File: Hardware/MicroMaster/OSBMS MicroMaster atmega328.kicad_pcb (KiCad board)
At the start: 2 copper layers, 33 parts, among them IC1 ATMEGA328P-A, P1 CONN_01X06, P10 CONN_01X04, P11 CONN_01X04, P2 CONN_02X03, P3 CONN_01X03, P4 CONN_01X03, P6 CONN_01X03, P7 CONN_01X02, P8 CONN_01X04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

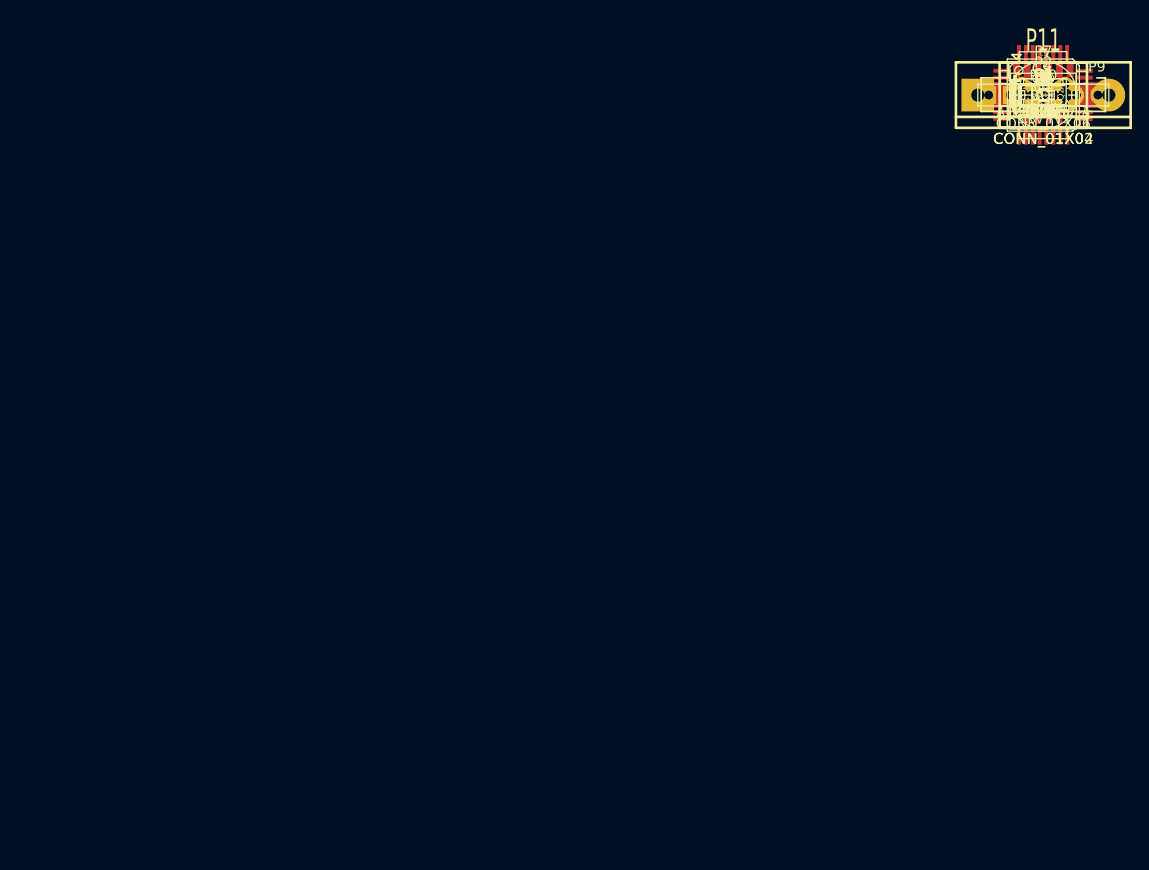
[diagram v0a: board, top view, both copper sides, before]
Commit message: touched up balancer board and reorganised
touched up balancer board so that it is ready for production,
reorganised a bunch of files and added proper revision labels, and made
good progress on the micromaster board. the schematic is complete, the
board is layed out, some traces still need to be run though.
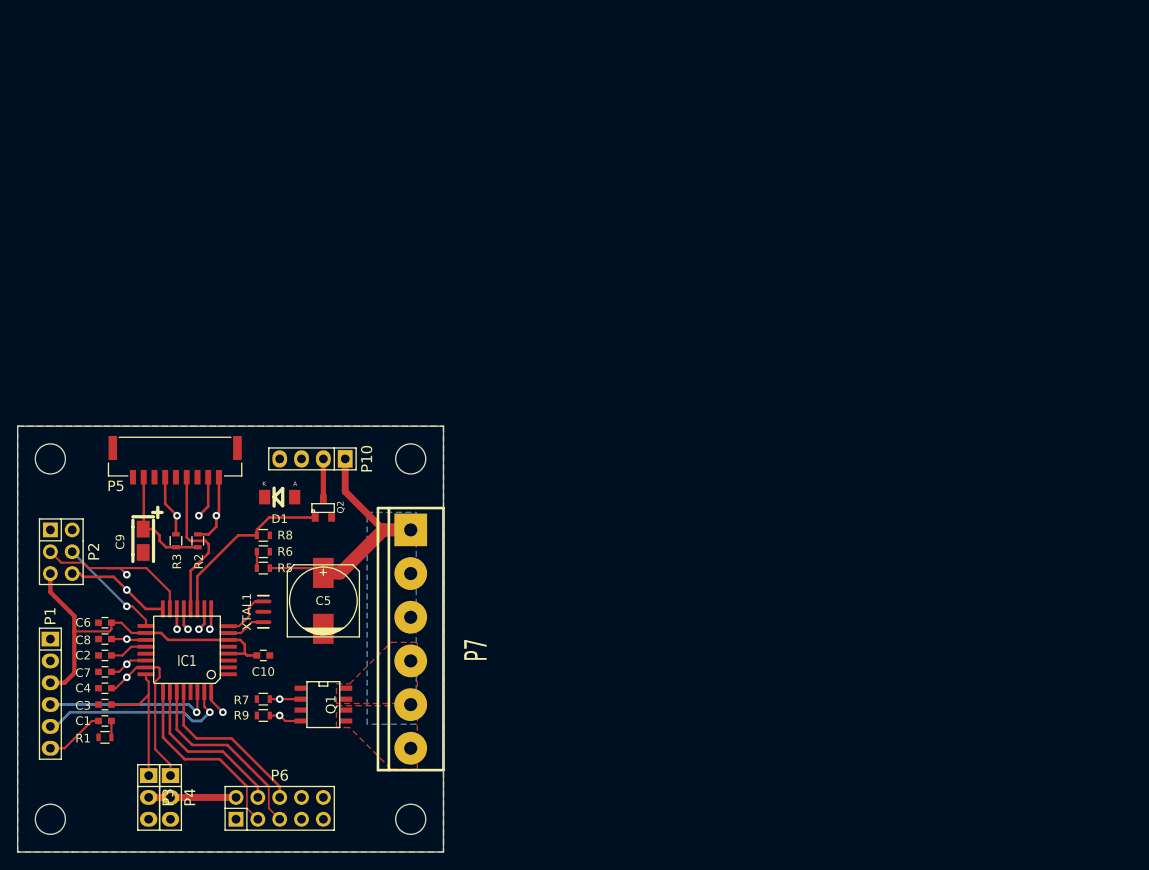
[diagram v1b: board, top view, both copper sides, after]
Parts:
- removed P11: CONN_01X04, Connect:bornier4
- removed P8: CONN_01X04, Pin_Headers:Pin_Header_Straight_1x04
- removed P9: CONN_01X06, Connectors_Molex:Connector_Molex_PicoBlade_53261-0671
- removed R4: 4.7K, Resistors_SMD:R_0603
- added MH: MountingHole_3-5mm_RevA_Date21Jun2010, Mounting_Holes:MountingHole_3-5mm, F.Cu at (71.1, 174.0)
- added MH: MountingHole_3-5mm_RevA_Date21Jun2010, Mounting_Holes:MountingHole_3-5mm, F.Cu at (29.2, 174.0)
- added MH: MountingHole_3-5mm_RevA_Date21Jun2010, Mounting_Holes:MountingHole_3-5mm, F.Cu at (29.2, 132.1)
- added MH: MountingHole_3-5mm_RevA_Date21Jun2010, Mounting_Holes:MountingHole_3-5mm, F.Cu at (71.1, 132.1)
- added P5: CONN_01X09, MyCustomParts:Connector_SMD_GH_SIDECONN_1X9_1.25MM_45515711ND, F.Cu at (43.8, 130.8)
- added XTAL1: 8mhz resonator, RESONATOR-SMD, F.Cu at (54.0, 149.9)
- D1: footprint SMD_Packages:DO-214-AC_SMA -> Diodes_SMD:Diode-MiniMELF_Standard
- IC1: footprint SMD_Packages:TQFP-32 -> TQFP-32
- P6: value CONN_01X03 -> CONN_01X10; footprint Pin_Headers:Pin_Header_Straight_1x03 -> Pin_Headers:Pin_Header_Straight_2x05
- P7: value CONN_01X02 -> CONN_01X06; footprint Connect:bornier2 -> Connect:bornier6
- moved P1 134.8 mm to (29.2, 159.4), turned to 270 degrees
- moved P3 132.3 mm to (40.6, 171.4), turned to 270 degrees
- moved R1 132.2 mm to (35.6, 164.5), turned to 180 degrees
- moved C1 131.2 mm to (35.6, 162.6)
- moved P4 130.3 mm to (43.2, 171.4), turned to 270 degrees
- moved C3 130.1 mm to (35.6, 160.7)
- moved C4 129.1 mm to (35.6, 158.8)
- moved C7 128.1 mm to (35.6, 156.8)
- moved C2 127.1 mm to (35.6, 154.9)
- moved C8 126.1 mm to (35.6, 153.0)
- moved P2 126.0 mm to (30.5, 142.9), turned to 270 degrees
- moved C6 125.2 mm to (35.6, 151.1)
- moved P6 121.5 mm to (55.9, 172.7)
- moved IC1 118.7 mm to (45.1, 154.3), turned to 180 degrees
- moved C9 116.8 mm to (40.0, 141.6), turned to 270 degrees
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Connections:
- C3 pad 2: /C_Sense1 -> A1
- C4 pad 2: /C_Sense2 -> A0
- C7 pad 2: A0 -> A7
- C8 pad 2: A1 -> A6
- D1 pad 1: A1 -> A6
- IC1 pad 12: D8 -> CS_N
- IC1 pad 15: MOSI/11* -> MOSI
- P10 pad 3: A1 -> A6
- P2 pad 1: MISO -> GND
- P2 pad 2: +3.3V -> RESET
- P2 pad 3: SCK/13 -> MOSI
- P2 pad 4: MOSI/11* -> SCK/13
- P2 pad 5: RESET -> +3.3V
- P2 pad 6: GND -> MISO
- P3 pad 1: /C_Sense1 -> A1
- P4 pad 1: /C_Sense2 -> A0
- P6 pad 1: /1WireComm -> GND
- P6 pad 2: Net-(P6-Pad2) -> +3.3V
- P6 pad 3: GND -> A2
- Q1 pad 5: Net-(P11-Pad4) -> Net-(P7-Pad6)
- Q1 pad 6: Net-(P11-Pad4) -> Net-(P7-Pad6)
- Q1 pad 7: Net-(P11-Pad2) -> Net-(P7-Pad4)
- Q1 pad 8: Net-(P11-Pad2) -> Net-(P7-Pad4)
- Q2 pad 1: D4 -> D7
- R5 pad 1: A0 -> A7
- R6 pad 2: A0 -> A7
- R8 pad 2: D4 -> D7
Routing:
- net +3.3V: track 0.00 -> 66.1 mm
- net +12V: track 0.00 -> 28.8 mm
- net MOSI: track 0.00 -> 25.5 mm, vias 0 -> 2
- net TXD: track 0.00 -> 22.7 mm, vias 0 -> 1
- net SDA/A4: track 0.00 -> 22.2 mm
- net A2: track 0.00 -> 21.8 mm
- net D7: track 0.00 -> 20.7 mm
- net MISO: track 0.00 -> 20.6 mm, vias 0 -> 2
- net A0: track 0.00 -> 20.0 mm, vias 0 -> 1
- net RXD: track 0.00 -> 19.8 mm, vias 0 -> 1
- net SCL/A5: track 0.00 -> 19.3 mm
- net A3: track 0.00 -> 18.9 mm
- net CS_N: track 0.00 -> 18.3 mm
- net A1: track 0.00 -> 16.9 mm
- net SCK/13: track 0.00 -> 12.6 mm, vias 0 -> 1
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- added copper zone on B.Cu, net +12V
- added copper zone on B.Cu, net GND
- added copper zone on F.Cu, net GND
- added copper zone on F.Cu, net Net-(P7-Pad4)
- added copper zone on F.Cu, net Net-(P7-Pad6)
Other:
- board outline added: 49.5 x 49.5 mm
- rule trace_min: 0.254 -> 0.127
- rule via_min_drill: 0.508 -> 0.3302
- rule via_min_size: 0.889 -> 0.508

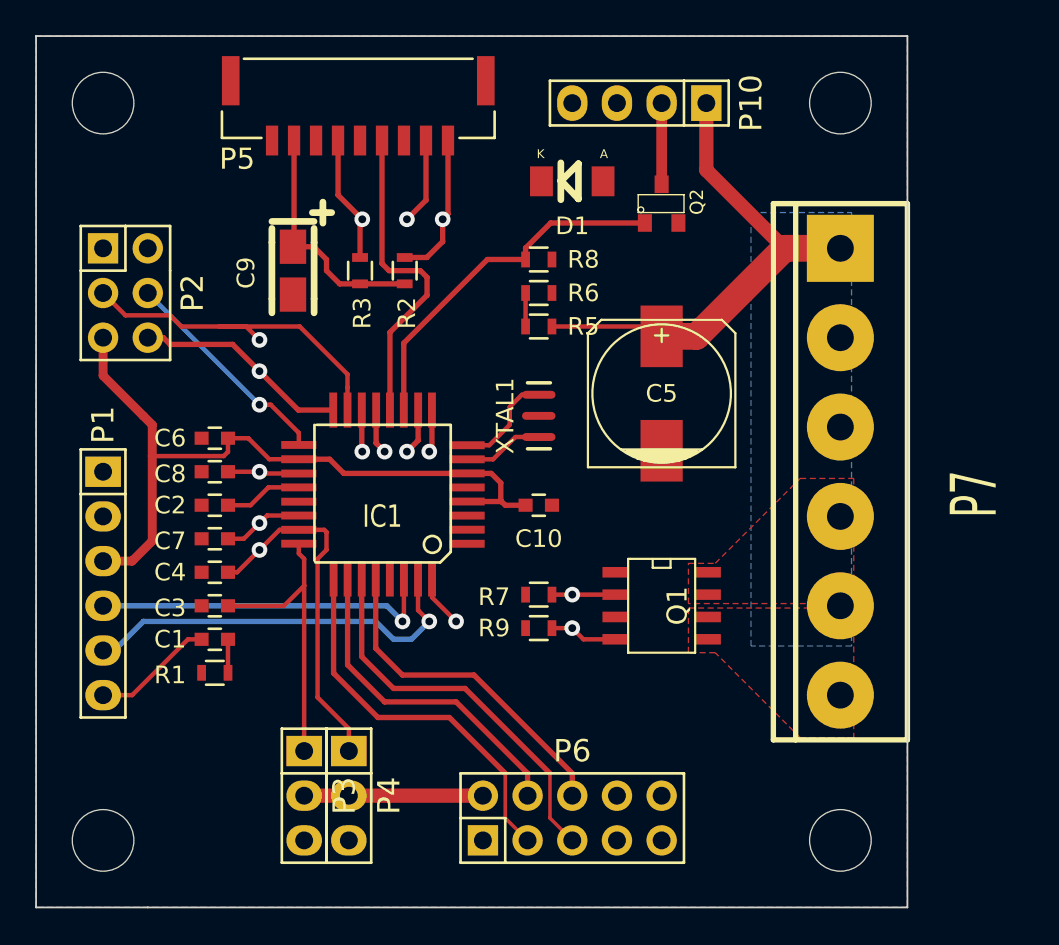
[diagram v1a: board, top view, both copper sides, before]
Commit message: Rev1 READY!
All the boards have been completed and arre ready for prototype
production. docunentation has been updated and the docs folder now
contains schematic pdf's, rendered pictures, and completed bill of
materials for both boarrds.

The software also recieved an update that corrected a datatype error and
shouuld make it testing ready.
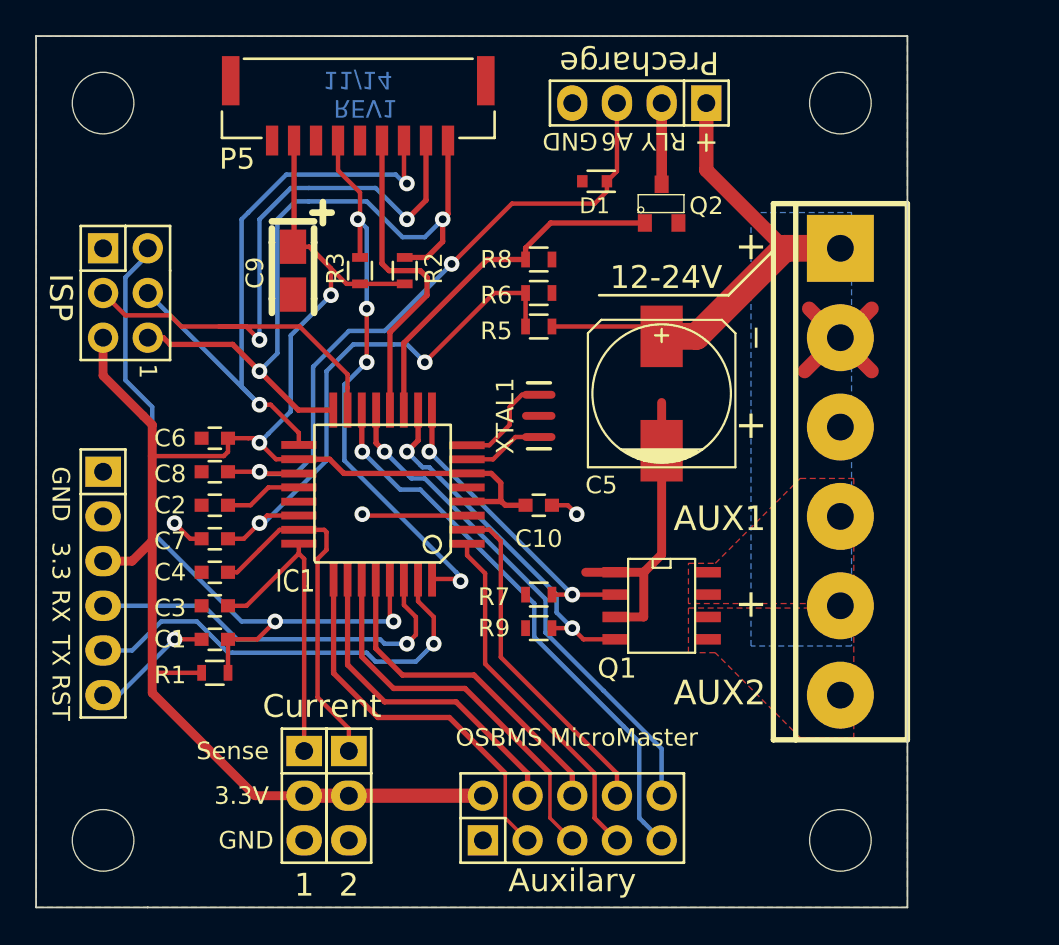
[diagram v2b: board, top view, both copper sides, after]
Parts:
- D1: value 3.3v TVS -> 3.3vZENER; footprint Diodes_SMD:Diode-MiniMELF_Standard -> SMD_Packages:SOD-523
- IC1: footprint TQFP-32 -> MyCustomParts:TQFP-32
- XTAL1: footprint RESONATOR-SMD -> MyCustomParts:RESONATOR-SMD-mutera
- moved D1 1.27 mm to (57.1, 136.5), turned to 0 degrees
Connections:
- D1 pad 1: A6 -> GND
- D1 pad 2: GND -> A6
- P6 pad 10: D10* -> D9*
- P6 pad 9: D9* -> D10*
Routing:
- net RESET: track 1.91 -> 40.6 mm, vias 0 -> 2
- net GND: track 0.00 -> 37.3 mm, vias 0 -> 3
- net +3.3V: track 66.1 -> 101.7 mm, vias 0 -> 2
- net A6: track 4.21 -> 38.9 mm, vias 1 -> 2
- net D10*: track 2.37 -> 32.2 mm
- net D9*: track 2.56 -> 29.1 mm
- net Int0/2: track 10.2 -> 35.1 mm, vias 2 -> 4
- net A7: track 6.48 -> 30.8 mm, vias 1 -> 2
- net SCK/13: track 12.6 -> 36.7 mm, vias 1 -> 2
- net D3*: track 0.00 -> 20.4 mm
- net MISO: track 20.6 -> 40.8 mm
- net D4: track 0.00 -> 19.4 mm
- net MOSI: track 25.5 -> 42.2 mm
- net D6*: track 6.46 -> 20.6 mm
- net D5*: track 5.99 -> 17.5 mm
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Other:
- board text added: "+"
- board text added: "1"
- board text added: "12-24V"
- board text added: "2"
- board text added: "3.3"
- board text added: "3.3V"
- board text added: "A6"
- board text added: "AUX1"
- board text added: "AUX2"
- board text added: "Auxilary"
- board text added: "Current"
- board text added: "GND"
- board text added: "ISP"
- board text added: "OSBMS MicroMaster"
- board text added: "Precharge"
- board text added: "REV1 11/14"
- board text added: "RLY"
- board text added: "RST"
- board text added: "RX"
- board text added: "Sense"
- board text added: "TX"
- board text added: "_"

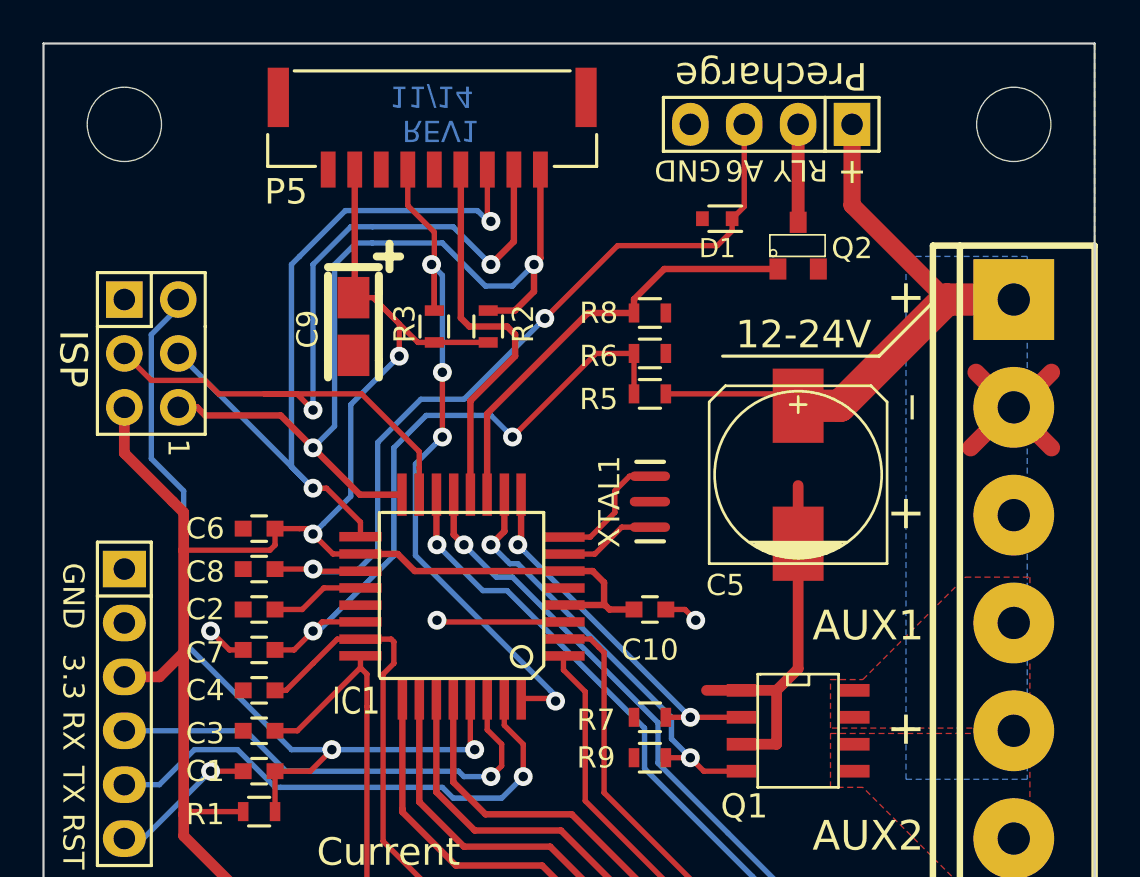
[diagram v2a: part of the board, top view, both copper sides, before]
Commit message: Finalised V1 for production
Finalised V1 for production. added hot symbol, moved mounting holes to
better location, fixed remaining drc error, and tiedied up silkscreen
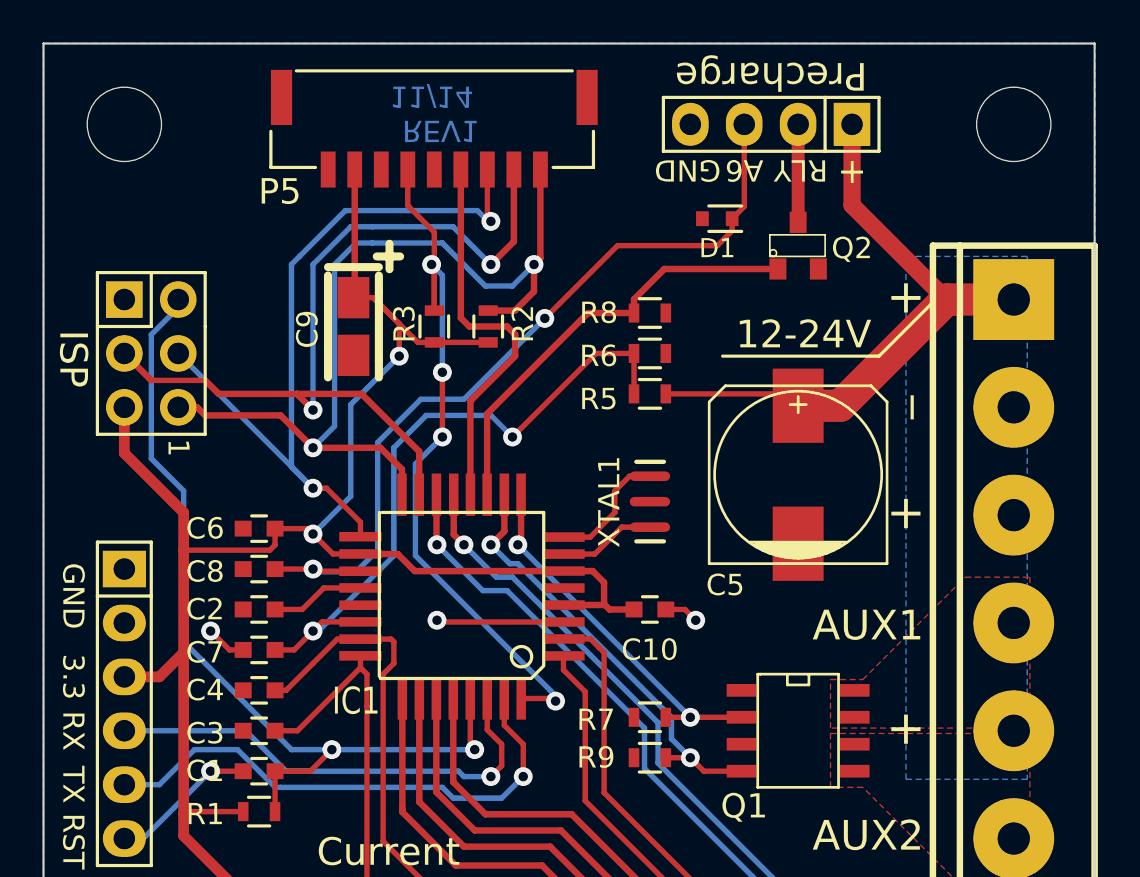
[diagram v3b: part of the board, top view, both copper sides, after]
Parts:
- P5: footprint MyCustomParts:Connector_SMD_GH_SIDECONN_1X9_1.25MM_45515711ND -> MyCustomParts:Connector_SMD_GH_SIDECONN_1X9_1.25MM
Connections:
- P5 pad : (no net) -> GND
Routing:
- net GND: track 37.3 -> 9.52 mm
- net MOSI: track 42.2 -> 40.6 mm
- net MISO: track 40.8 -> 41.5 mm

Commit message: work dump
board schematics should be working. may include some unfinished
schematics and software pieces
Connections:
- IC1 pad 13: D9* -> 400khz_clk
- P1 pad : GND -> (no net)
- P5 pad : GND -> (no net)
- P5 pad 5: Net-(P5-Pad5) -> 400khz_clk
- P6 pad 10: D9* -> (no net)
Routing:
- net D9*: track 29.1 -> 0.00 mm, vias 1 -> 0
- net 400khz_clk: track 0.00 -> 29.1 mm, vias 0 -> 1
